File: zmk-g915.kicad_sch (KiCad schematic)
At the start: 43 parts, among them J1 Prog_conn, J2 Tag connect TC2030-CTX, SW1 Reset Switch, U1 nRF52840-QIAA-R/nRF52833-QIAA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, Y1 32.768kHz, Y2 32MHz

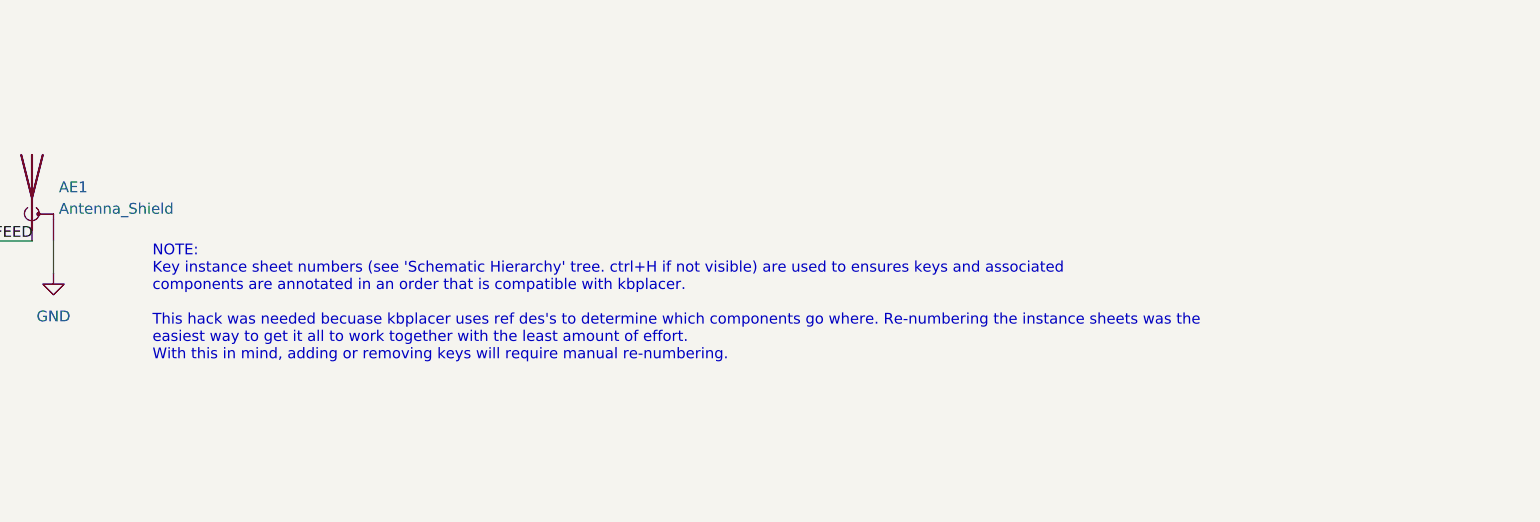
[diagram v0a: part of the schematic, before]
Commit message: created dev-board to prove design before full-size
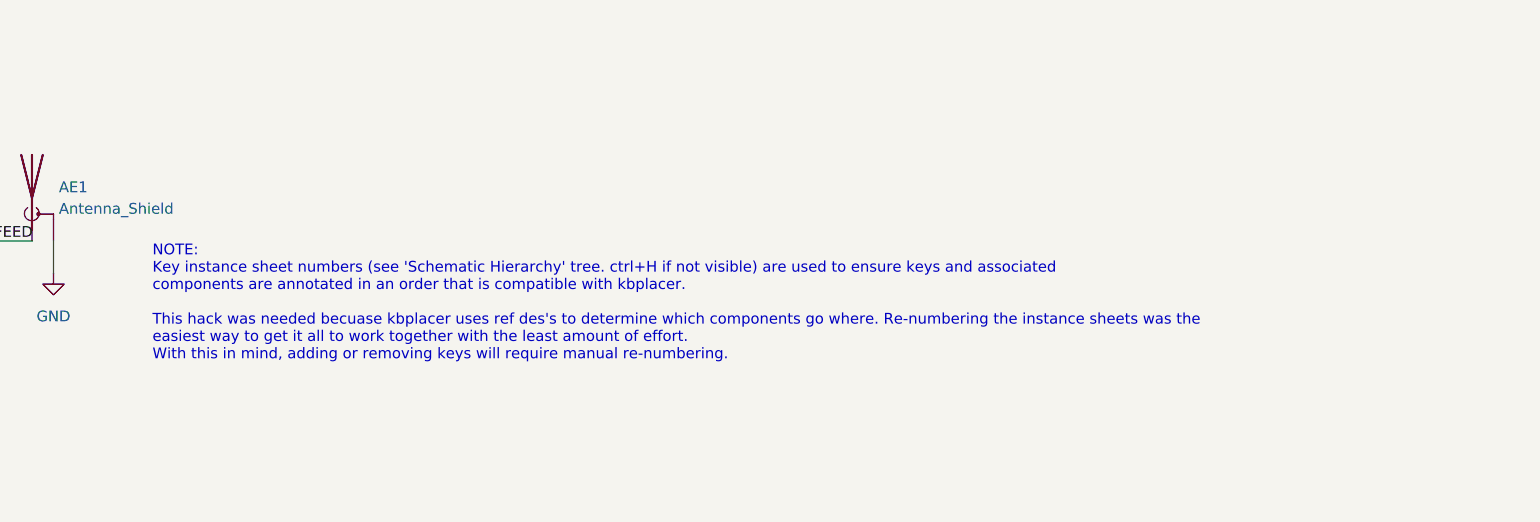
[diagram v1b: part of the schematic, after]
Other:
- note added: "NOTE: Key instance sheet numbers (see 'Schematic Hierarchy' tree. ctrl+H if not visible) are used to ensure keys and associated components are annotated in an order that is compatible with kbplacer. This hack was needed becuase kbplacer uses ref des's to determine which components go where. Re-numbering the instance sheets was the easiest way to get it all to work together with the least amount o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"
- note removed: "NOTE: Key instance sheet numbers (see 'Schematic Hierarchy' tree. ctrl+H if not visible) are used to ensures keys and associated components are annotated in an order that is compatible with kbplacer. This hack was needed becuase kbplacer uses ref des's to determine which components go where. Re-numbering the instance sheets was the easiest way to get it all to work together with the least amount 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"
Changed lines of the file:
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@@
 		)
 	)
-	(text "NOTE:\nKey instance sheet numbers (see 'Schematic Hierarchy' tree. ctrl+H if not visible) are used to ensures keys and associated\ncomponents are annotated in an order that is compatible with kbplacer.\n\nThis hack was needed becuase kbplacer uses ref des's to determine which components go where. Re-numbering the instance sheets was the\neasiest way to get it all to work together with the least amount of effort.\nWith this in mind, adding or removing keys will require manual re-numbering."
+	(text "NOTE:\nKey instance sheet numbers (see 'Schematic Hierarchy' tree. ctrl+H if not visible) are used to ensure keys and associated\ncomponents are annotated in an order that is compatible with kbplacer.\n\nThis hack was needed becuase kbplacer uses ref des's to determine which components go where. Re-numbering the instance sheets was the\neasiest way to get it all to work together with the least amount of effort.\nWith this in mind, adding or removing keys will require manual re-numbering."
 		(exclude_from_sim no)
 		(at 178.054 173.736 0)
